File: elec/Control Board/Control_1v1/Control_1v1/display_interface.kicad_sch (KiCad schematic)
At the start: 4 parts, among them J35 Conn_02x05_Odd_Even, J36 Conn_02x05_Odd_Even

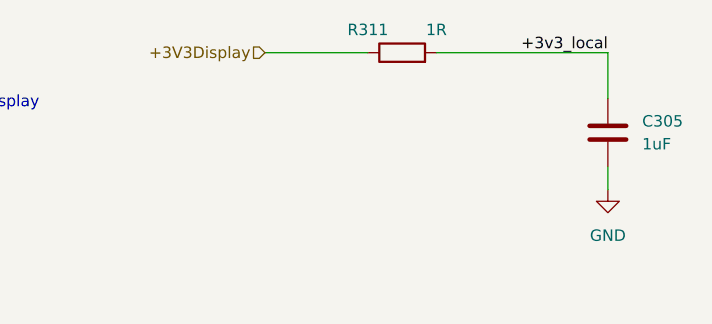
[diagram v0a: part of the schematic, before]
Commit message: unified 1R and 1R0 references
Signed-off-by: lokimetasmith <lokimail@gmail.com>
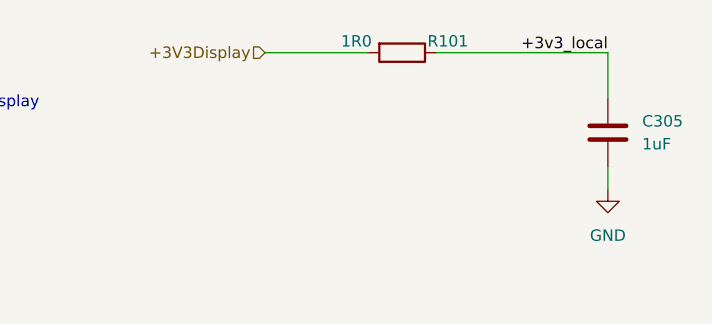
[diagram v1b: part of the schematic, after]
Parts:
- removed R311: 1R, Resistor_SMD:R_0603_1608Metric_Pad0.98x0.95mm_HandSolder, symbol Device:R
- added R101: 1R0, Resistor_SMD:R_0603_1608Metric_Pad0.98x0.95mm_HandSolder, symbol Device:R
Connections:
- net +3V3Display: now also R101.2
- net +3v3_local: now also R101.1
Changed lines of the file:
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@@
     )
   )
-  (symbol (lib_id "Device:R") (at 220.98 27.94 90) (unit 1)
+  (symbol (lib_id "Device:R") (at 220.98 27.94 270) (unit 1)
     (in_bom yes) (on_board yes) (dnp no)
-    (property "Reference" "R311" (at 217.17 25.4 90)
+    (property "Reference" "R101" (at 226.06 26.67 90)
       (effects (font (size 1.27 1.27)))
     )
-    (property "Value" "1R" (at 224.79 25.4 90)
+    (property "Value" "1R0" (at 215.9 26.67 90)
       (effects (font (size 1.27 1.27)))
     )
-    (property "Footprint" "Resistor_SMD:R_0603_1608Metric_Pad0.98x0.95mm_HandSolder" (at 220.98 29.718 90)
+    (property "Footprint" "Resistor_SMD:R_0603_1608Metric_Pad0.98x0.95mm_HandSolder" (at 220.98 26.162 90)
       (effects (font (size 1.27 1.27)) hide)
     )
@@
       (effects (font (size 1.27 1.27)) hide)
     )
-    (property "AssemblyType" "SMT" (at 220.98 27.94 0)
+    (property "Distributor 1" "JLCPCB" (at 220.98 27.94 90)
       (effects (font (size 1.27 1.27)) hide)
     )
-    (property "Distributor 1" "NA" (at 220.98 27.94 0)
+    (property "Distributor 1 PN" "C269434" (at 220.98 27.94 90)
       (effects (font (size 1.27 1.27)) hide)
     )
-    (property "Distributor 1 PN" "NA" (at 220.98 27.94 0)
+    (property "Manufacturer" "TyoHM" (at 220.98 27.94 90)
+      (effects (font (size 1.27 1.27)) hide)
+    )
+    (property "MPN" "RMC060315%N" (at 220.98 27.94 90)
+      (effects (font (size 1.27 1.27)) hide)
+    )
+    (property "Description" "0.1W ±5% 1Ω 0603 Chip Resistor - Surface Mount ROHS" (at 220.98 27.94 0)
+      (effects (font (size 1.27 1.27)) hide)
+    )
+    (property "AssemblyType" "SMT" (at 220.98 27.94 0)
       (effects (font (size 1.27 1.27)) hide)
     )
@@
       (effects (font (size 1.27 1.27)) hide)
     )
-    (property "Description" "Do Not Insert" (at 220.98 27.94 0)
-      (effects (font (size 1.27 1.27)) hide)
-    )
     (pin "1")
     (pin "2")
     (instances
-      (project "fan_I2C"
-        (path "/27e09928-2db5-4ece-9e90-f2a9a0b91b8d/2799eafe-5d1a-4095-9bfc-d8b3526b9754"
-          (reference "R311") (unit 1)
+      (project "GeneralPurposeAlarmDevicePCB"
+        (path "/412a327d-1ee3-473e-bc00-1545004b7edf"
+          (reference "R101") (unit 1)
         )
       )
       (project "Control_1v1"
-        (path "/c68c9deb-8d4d-42f0-adf8-4d3022f4ee59/1f0b18fc-1fda-489e-a08b-a0ece1be6922"
-          (reference "R59") (unit 1)
+        (path "/c68c9deb-8d4d-42f0-adf8-4d3022f4ee59/0cb2f0dc-fe38-451d-b752-5d12a98f8d03"
+          (reference "R9") (unit 1)
+        )
+        (path "/c68c9deb-8d4d-42f0-adf8-4d3022f4ee59"
+          (reference "R144") (unit 1)
+        )
+        (path "/c68c9deb-8d4d-42f0-adf8-4d3022f4ee59/3ff32a52-b1ed-4756-8661-90a95f721605"
+          (reference "R7") (unit 1)
+        )
+        (path "/c68c9deb-8d4d-42f0-adf8-4d3022f4ee59/3daed20d-8623-449a-af6f-871db7628ab2"
+          (reference "R20") (unit 1)
         )
         (path "/c68c9deb-8d4d-42f0-adf8-4d3022f4ee59/f2cc20dc-f81b-4e9e-a9e1-88ed6ea8264c"

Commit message: Move components away from J35, J36.
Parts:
- J35, J36: footprint Connector_PinHeader_2.54mm:PinHeader_2x05_P2.54mm_Vertical -> Connector_IDC:IDC-Header_2x05_P2.54mm_Vertical
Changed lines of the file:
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@@
       (effects (font (size 1.27 1.27)) (justify right))
     )
-    (property "Footprint" "Connector_PinHeader_2.54mm:PinHeader_2x05_P2.54mm_Vertical" (at 134.62 58.42 0)
+    (property "Footprint" "Connector_IDC:IDC-Header_2x05_P2.54mm_Vertical" (at 134.62 58.42 0)
       (effects (font (size 1.27 1.27)) hide)
     )
@@
       (effects (font (size 1.27 1.27)) (justify right))
     )
-    (property "Footprint" "Connector_PinHeader_2.54mm:PinHeader_2x05_P2.54mm_Vertical" (at 78.74 58.42 0)
+    (property "Footprint" "Connector_IDC:IDC-Header_2x05_P2.54mm_Vertical" (at 78.74 58.42 0)
       (effects (font (size 1.27 1.27)) hide)
     )

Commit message: Add Breadboard30P.
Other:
- company: (none) -> Public Invention
- title: (none) -> Control Interconnect Board OEDCS
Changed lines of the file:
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@@
 (kicad_sch (version 20230121) (generator eeschema)
   (paper "A4")
+  (title_block
+    (title "Control Interconnect Board OEDCS")
+    (date "2023-10-10")
+    (rev "Rev 1.1")
+    (company "Public Invention")
+    (comment 1 "GNU Affero General Public License v3.0")
+    (comment 2 "Contributor: Lawrence Kinceloe")
+    (comment 3 "Drawn By: (Forrest) Lee Erickson")
+  )
   (wire (pts (xy 205.74 27.94) (xy 217.17 27.94))
     (stroke (width 0) (type default))
